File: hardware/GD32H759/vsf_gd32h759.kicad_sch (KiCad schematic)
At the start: 107 parts, among them J1 Micro_SD_Card_Det1, J2 USB_C_Receptacle_USB2.0, J3 USB_A, J4 USB_C_Receptacle_USB2.0, SW1 SW_Push, SW2 SW_Push, SW3 SW_Push, SW4 SW_Push, U1 GD32H759_LQFP176, U2 MT48LC16M16A2TG, U3 CH340N, U4 ETA9638, U5 ETA3486, Y1 25M, Y2 32.768KHz

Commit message: [hw/gd32h759] update
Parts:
- added C56, C57, C58: 1uF, Capacitor_SMD:C_0402_1005Metric, symbol Device:C
- added C59: 0.1uF, Capacitor_SMD:C_0402_1005Metric, symbol Device:C
- added D3: 1N4148, Diode_SMD:D_SOD-523, symbol Diode:1N4148
- added J10, J11: Conn_01x06, symbol Connector_Generic:Conn_01x06
- added J5, J6: Conn_02x32_Odd_Even, symbol Connector_Generic:Conn_02x32_Odd_Even
- added J7: PJ-393-USA, VSF:PJ-393, symbol VSF:PJ-393-USA
- added J8: LS035Y8DX02A, symbol Connector_Generic:Conn_02x25_Counter_Clockwise
- added J9: Conn_01x40, symbol Connector_Generic:Conn_01x40
- added Q1: PMBT3904, Package_TO_SOT_SMD:SOT-23, symbol Device:Q_NPN_BEC
- added R30, R31, R32: 4.7K, Resistor_SMD:R_0402_1005Metric, symbol Device:R
- added R33: 100K, Resistor_SMD:R_0402_1005Metric, symbol Device:R
- added R34: 1K, Resistor_SMD:R_0402_1005Metric, symbol Device:R
- added R35: 2.2K, Resistor_SMD:R_0402_1005Metric, symbol Device:R
- added R36: 2K, Resistor_SMD:R_0402_1005Metric, symbol Device:R
- added R37, R38, R39, R40, R41, R42: NC, Resistor_SMD:R_0402_1005Metric, symbol Device:R
- added SW5: SW_Push, VSF:Key_2Pin_2.9X4.3, symbol Switch:SW_Push
- added U6: CS4265, Package_DFN_QFN:QFN-32-1EP_5x5mm_P0.5mm_EP3.6x3.6mm, symbol Audio:CS4265
- added U7: ~, symbol VSF:AIC8800D40L_SDIO_Module
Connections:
- net GND: now also C56.1, J10.4 (Pin_4), J11.4 (Pin_4), J5.1 (Pin_1), J6.1 (Pin_1), J7.4, J8.1 (Pin_1), J8.14 (Pin_14), J8.23 (Pin_23), J8.25 (Pin_25), J8.26 (Pin_26), J8.28 (Pin_28), J8.30 (Pin_30), J8.41 (Pin_41), J8.5 (Pin_5), J8.50 (Pin_50), J9.29 (Pin_29), J9.3 (Pin_3), J9.36 (Pin_36)
- net NRST: now also J5.3 (Pin_3)
- net PWR_3V3: now also J5.2 (Pin_2)
- net UART_RX: now also D3.2 (A), R30.2; no longer U3.6 (TXD)
- net UART_TX: now also Q1.2 (E); no longer U3.7 (RXD)
- net USB5V_OUT: now also J6.2 (Pin_2)
- net VBAT: now also J5.4 (Pin_4)
- net VDD: now also J10.1 (Pin_1), J11.1 (Pin_1), J8.2 (Pin_2), J8.3 (Pin_3), J8.4 (Pin_4), J9.4 (Pin_4), R37.2, R38.2, SW5.2
- net VREF: now also J6.3 (Pin_3)
- net PA0: now reaches U1.41 (PA0)
- net PA0: now also SW5.1
- new net: C59.2, J7.1, J7.8, R35.1
- new net: C56.2, R34.1, R35.2
- new net: J9.31 (Pin_31), R37.1
- new net: J9.35 (Pin_35), R38.1
- new net: J9.37 (Pin_37), R39.1
- new net: J9.38 (Pin_38), R40.1
- new net: J9.39 (Pin_39), R41.1
- new net: J9.40 (Pin_40), R42.1
- new net: Q1.3 (C), R31.1, U3.7 (RXD)
- new net: J7.7, R36.1
- new net: C57.2, J7.3, J7.6
- new net: D3.1 (K), U3.6 (TXD)
- new net: Q1.1 (B), R32.1
- new net: C58.2, J7.2, J7.5
- new net: U6.18 (AGND), U6.33 (AGND), U6.6 (AGND)
- new net HPLP: C58.1
- new net HPRP: C57.1
- new net JACK_DET: R33.1, R36.2
- new net LCD_CS: J8.36 (Pin_36), R40.2
- new net LCD_MISO: J8.39 (Pin_39)
- new net LCD_MOSI: J8.38 (Pin_38), R42.2
- new net LCD_RST: J8.40 (Pin_40), R39.2
- new net LCD_SCK: J8.37 (Pin_37), R41.2
- new net LED+: J9.2 (Pin_2)
- new net LED-: J9.1 (Pin_1)
- new net LEDA: J8.29 (Pin_29)
- new net LEDC: J8.27 (Pin_27)
- new net LEDPWM: J8.24 (Pin_24)
- new net MARKER_ID: J8.31 (Pin_31)
- new net MIC_BIAS: R34.2
- new net MIC_INP: C59.1
- new net TLI_B0: J8.6 (Pin_6), J9.21 (Pin_21)
- new net TLI_B1: J8.7 (Pin_7), J9.22 (Pin_22)
- new net TLI_B2: J8.8 (Pin_8), J9.23 (Pin_23)
- new net TLI_B3: J8.9 (Pin_9), J9.24 (Pin_24)
- new net TLI_B4: J8.10 (Pin_10), J9.25 (Pin_25)
- new net TLI_B5: J8.11 (Pin_11), J9.26 (Pin_26)
- new net TLI_B6: J8.12 (Pin_12), J9.27 (Pin_27)
- new net TLI_B7: J8.13 (Pin_13), J9.28 (Pin_28)
- new net TLI_DE: J8.32 (Pin_32), J9.34 (Pin_34)
- new net TLI_G0: J8.15 (Pin_15), J9.13 (Pin_13)
- new net TLI_G1: J8.16 (Pin_16), J9.14 (Pin_14)
- new net TLI_G2: J8.17 (Pin_17), J9.15 (Pin_15)
- new net TLI_G3: J8.18 (Pin_18), J9.16 (Pin_16)
- new net TLI_G4: J8.19 (Pin_19), J9.17 (Pin_17)
- new net TLI_G5: J8.20 (Pin_20), J9.18 (Pin_18)
- new net TLI_G6: J8.21 (Pin_21), J9.19 (Pin_19)
- new net TLI_G7: J8.22 (Pin_22), J9.20 (Pin_20)
- new net TLI_HSYNC: J8.33 (Pin_33), J9.32 (Pin_32)
- new net TLI_PCLK: J8.35 (Pin_35), J9.30 (Pin_30)
- new net TLI_R0: J8.42 (Pin_42), J9.5 (Pin_5)
- new net TLI_R1: J8.43 (Pin_43), J9.6 (Pin_6)
- new net TLI_R2: J8.44 (Pin_44), J9.7 (Pin_7)
- new net TLI_R3: J8.45 (Pin_45), J9.8 (Pin_8)
- new net TLI_R4: J8.46 (Pin_46), J9.9 (Pin_9)
- new net TLI_R5: J8.47 (Pin_47), J9.10 (Pin_10)
- new net TLI_R6: J8.48 (Pin_48), J9.11 (Pin_11)
- new net TLI_R7: J8.49 (Pin_49), J9.12 (Pin_12)
- new net TLI_VSYNC: J8.34 (Pin_34), J9.33 (Pin_33)
- new net TS_INT: J10.6 (Pin_6), J11.6 (Pin_6)
- new net TS_RST: J10.5 (Pin_5), J11.5 (Pin_5)
- new net TS_SCL: J10.3 (Pin_3), J11.3 (Pin_3)
- new net TS_SDA: J10.2 (Pin_2), J11.2 (Pin_2)
- new net USB5V: R31.2
- new net VCC: R30.1, R32.2, R33.2
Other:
- moved on the sheet: C47, J1, R21, R22, R23, R24, R25

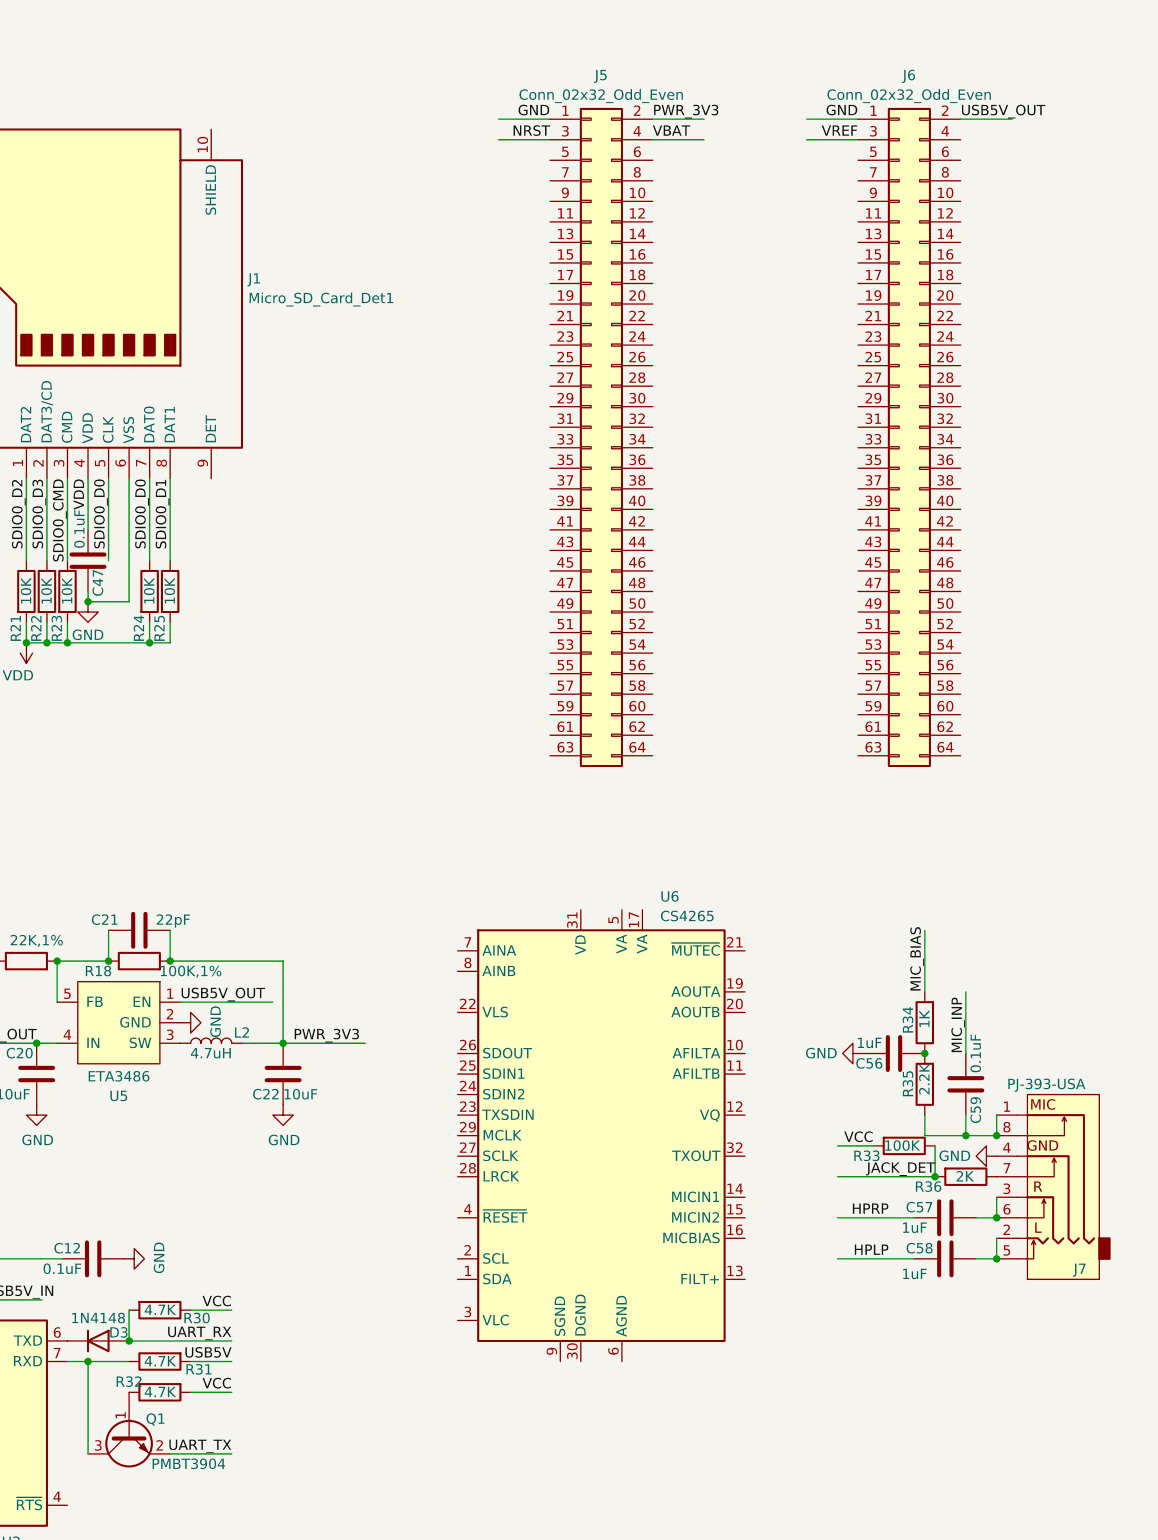
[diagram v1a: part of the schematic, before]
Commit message: [hardware/gd32h759] envaluate pcb size
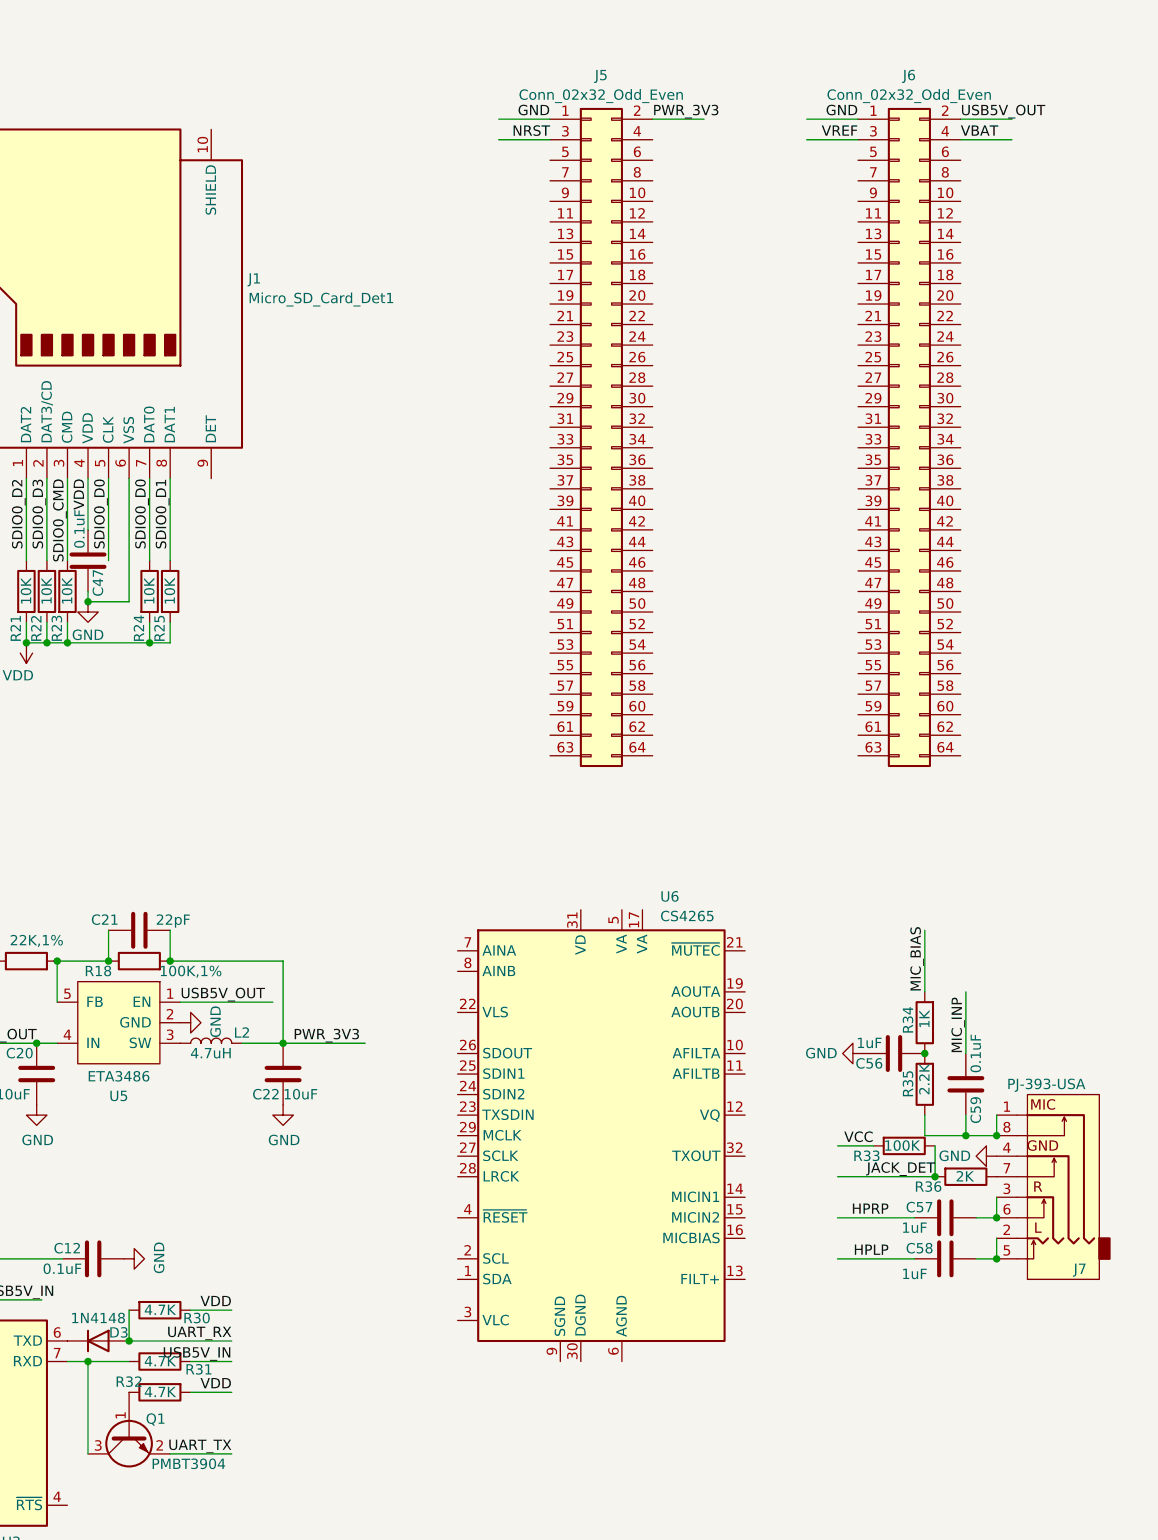
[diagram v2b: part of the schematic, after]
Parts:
- J5, J6: footprint (none) -> Connector_PinHeader_2.54mm:PinHeader_2x32_P2.54mm_Vertical
- SW1, SW2, SW3: footprint VSF:Key_2Pin_2.9X4.3 -> VSF:JHA004
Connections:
- net USB5V is gone; now on net USB5V_IN: R31.2
- net VBAT: now also J6.4 (Pin_4); no longer J5.4 (Pin_4)
- net VCC: no longer R30.1, R32.2
- net VDD: now also R30.1, R32.2
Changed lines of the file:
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@@
 	(wire
 		(pts
+			(xy 374.65 34.29) (xy 381 34.29)
+		)
+		(stroke
+			(width 0)
+			(type default)
+		)
+	)
+	(wire
+		(pts
 			(xy 129.54 49.53) (xy 132.08 49.53)
 		)
@@
 	(wire
 		(pts
-			(xy 336.55 34.29) (xy 342.9 34.29)
-		)
-		(stroke
-			(width 0)
-			(type default)
-		)
-	)
-	(wire
-		(pts
 			(xy 43.18 243.84) (xy 39.37 243.84)
 		)
@@
 		)
 	)
-	(label "VCC"
+	(label "VDD"
 		(at 284.48 189.23 180)
 		(fields_autoplaced yes)
@@
 		)
 	)
-	(label "VBAT"
-		(at 336.55 34.29 0)
-		(fields_autoplaced yes)
-		(effects
-			(font
-				(size 1.27 1.27)
-			)
-			(justify left bottom)
-		)
-	)
 	(label "MIC_INP"
 		(at 375.285 147.32 90)
@@
 		)
 	)
-	(label "USB5V"
+	(label "USB5V_IN"
 		(at 284.48 185.42 180)
 		(fields_autoplaced yes)
@@
 		)
 	)
+	(label "VBAT"
+		(at 374.65 34.29 0)
+		(fields_autoplaced yes)
+		(effects
+			(font
+				(size 1.27 1.27)
+			)
+			(justify left bottom)
+		)
+	)
 	(label "GND"
 		(at 514.35 127 0)
@@
 		)
 	)
-	(label "VCC"
+	(label "VDD"
 		(at 284.48 179.07 180)
 		(fields_autoplaced yes)
@@
 			)
 		)
-		(property "Footprint" ""
+		(property "Footprint" "Connector_PinHeader_2.54mm:PinHeader_2x32_P2.54mm_Vertical"
 			(at 328.93 69.85 0)
 			(effects
@@
 			)
 		)
-		(property "Footprint" "VSF:Key_2Pin_2.9X4.3"
+		(property "Footprint" "VSF:JHA004"
 			(at 198.12 111.76 0)
 			(effects
@@
 			)
 		)
-		(property "Footprint" "VSF:Key_2Pin_2.9X4.3"
+		(property "Footprint" "VSF:JHA004"
 			(at 35.56 63.5 0)
 			(effects
@@
 			)
 		)
-		(property "Footprint" ""
+		(property "Footprint" "Connector_PinHeader_2.54mm:PinHeader_2x32_P2.54mm_Vertical"
 			(at 367.03 69.85 0)
 			(effects
@@
 			)
 		)
-		(property "Footprint" "VSF:Key_2Pin_2.9X4.3"
+		(property "Footprint" "VSF:JHA004"
 			(at 204.47 118.11 0)
 			(effects
